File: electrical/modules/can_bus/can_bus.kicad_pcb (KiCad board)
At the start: 2 copper layers, 8 parts, among them U101 TCAN330DR

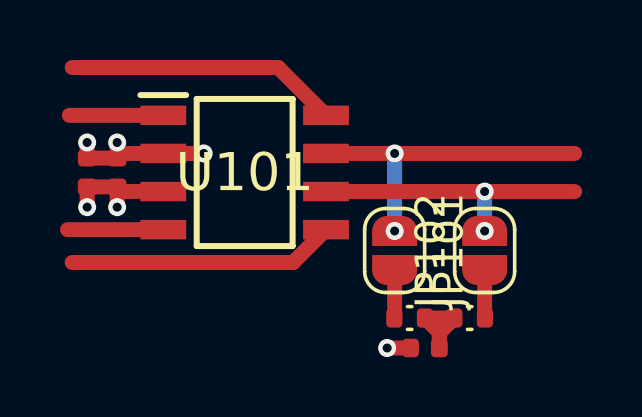
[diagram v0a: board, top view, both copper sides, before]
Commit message: Update CAN bus module and connect it.
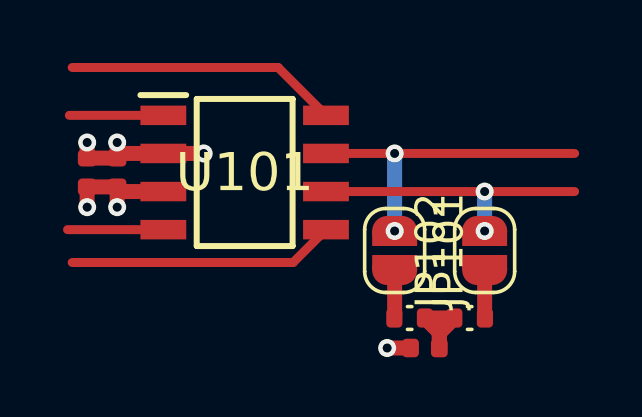
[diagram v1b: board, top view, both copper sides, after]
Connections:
- net +3V3 renamed /3V3
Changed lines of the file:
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@@
 	(net 0 "")
 	(net 1 "GND")
-	(net 2 "+3V3")
+	(net 2 "/3V3")
 	(net 3 "/CANH_TERMINATION")
 	(net 4 "/CANL_TERMINATION")
@@
 			(size 0.65 1.528)
 			(layers "F.Cu" "F.Mask" "F.Paste")
-			(net 2 "+3V3")
+			(net 2 "/3V3")
 			(pinfunction "VCC")
 			(pintype "passive")
@@
 			(layers "F.Cu" "F.Mask" "F.Paste")
 			(roundrect_rratio 0.25)
-			(net 2 "+3V3")
+			(net 2 "/3V3")
 			(pintype "passive")
 		)
@@
 			(layers "F.Cu" "F.Mask" "F.Paste")
 			(roundrect_rratio 0.25)
-			(net 2 "+3V3")
+			(net 2 "/3V3")
 			(pintype "passive")
 		)
@@
 		(start 144.339 98.58)
 		(end 141.145 98.58)
-		(width 0.5)
+		(width 0.3)
 		(layer "F.Cu")
 		(net 5)
@@
 		(start 148.166 93.175)
 		(end 141.3 93.175)
-		(width 0.5)
+		(width 0.3)
 		(layer "F.Cu")
 		(net 6)
@@
 		(start 149.761 94.77)
 		(end 148.166 93.175)
-		(width 0.5)
+		(width 0.3)
 		(layer "F.Cu")
 		(net 6)
@@
 		(start 149.761 98.58)
 		(end 148.666 99.675)
-		(width 0.5)
+		(width 0.3)
 		(layer "F.Cu")
 		(net 7)
@@
 		(start 148.666 99.675)
 		(end 141.3 99.675)
-		(width 0.5)
+		(width 0.3)
 		(layer "F.Cu")
 		(net 7)
@@
 		(start 144.339 94.77)
 		(end 141.205 94.77)
-		(width 0.5)
+		(width 0.3)
 		(layer "F.Cu")
 		(net 8)
@@
 		(start 152.05 96.04)
 		(end 158.05 96.04)
-		(width 0.5)
+		(width 0.3)
 		(layer "F.Cu")
 		(net 10)
@@
 		(start 149.761 96.04)
 		(end 152.05 96.04)
-		(width 0.5)
+		(width 0.3)
 		(layer "F.Cu")
 		(net 10)
@@
 		(start 155.05 97.31)
 		(end 158.05 97.31)
-		(width 0.5)
+		(width 0.3)
 		(layer "F.Cu")
 		(net 11)
@@
 		(start 149.761 97.31)
 		(end 155.05 97.31)
-		(width 0.5)
+		(width 0.3)
 		(layer "F.Cu")
 		(net 11)

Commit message: Complete fanout of CAN bus controller and related passive components.
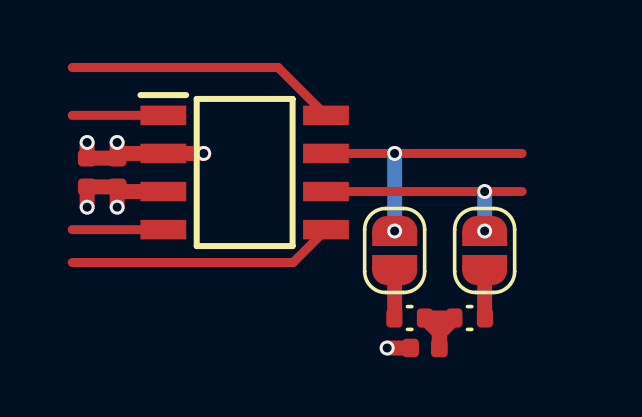
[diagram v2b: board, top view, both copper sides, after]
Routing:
- net /CANL: track 9.60 -> 7.85 mm
- net /CANH: track 10.9 -> 9.12 mm
- added copper zone on In2.Cu, net /3V3
- added copper zone on In1.Cu, net GND
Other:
- copper layers 2 -> 4

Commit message: Checkpoint work on building core board module.
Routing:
- net /CAN_SILENT: track 9.12 -> 6.66 mm
- net /CAN_SHUTDOWN: track 8.91 -> 6.66 mm
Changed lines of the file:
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@@
 	)
 	(segment
-		(start 148.166 93.175)
-		(end 141.3 93.175)
+		(start 149.761 94.77)
+		(end 148.666 93.675)
 		(width 0.3)
 		(layer "F.Cu")
@@
 	)
 	(segment
-		(start 149.761 94.77)
-		(end 148.166 93.175)
+		(start 148.666 93.675)
+		(end 143.55 93.675)
 		(width 0.3)
 		(layer "F.Cu")
@@
 	(segment
 		(start 148.666 99.675)
-		(end 141.3 99.675)
+		(end 143.55 99.675)
 		(width 0.3)
 		(layer "F.Cu")

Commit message: Restructure modules to get a reasonable core_board module.
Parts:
- C101, C102, C103, JP101, JP102, R101, R102, U101: moved to B.Cu
- moved C101 15.2 mm to (157.0, 96.7)
- moved C102 13.2 mm to (156.0, 96.7)
- moved JP102 11.3 mm to (143.8, 99.3)
- moved R102 10.3 mm to (144.3, 101.5), turned to 180 degrees
- moved C103 7.27 mm to (145.8, 102.5), turned to 180 degrees
- moved R101 6.25 mm to (146.3, 101.5), turned to 180 degrees
- moved JP101 5.25 mm to (146.8, 99.3)
- moved U101 4.75 mm to (151.8, 96.7), turned to 180 degrees

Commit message: Start sequence to synchronize UUIDs in modules so that ProjectInstances doesn't fail to import PCB layout.
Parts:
- renumbered C101 to C701, C102 to C702, C103 to C703, JP101 to JP701, JP102 to JP702, R101 to R701, R102 to R702, U101 to U701
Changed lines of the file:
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@@
 	(net 7 "/CAN_SHUTDOWN")
 	(net 8 "/CAN_TX")
-	(net 9 "Net-(C103-Pad2)")
+	(net 9 "Net-(C703-Pad2)")
 	(net 10 "/CANH")
 	(net 11 "/CANL")
@@
 		(descr "Capacitor SMD 0402 (1005 Metric), square (rectangular) end terminal, IPC_7351 nominal, (Body size source: IPC-SM-782 page 76, https://www.pcb-3d.com/wordpress/wp-content/uploads/ipc-sm-782a_amendment_1_and_2.pdf), generated with kicad-footprint-generator")
 		(tags "capacitor")
-		(property "Reference" "C103"
+		(property "Reference" "C703"
 			(at 0 1.16 0)
 			(layer "B.SilkS")
@@
 			(layers "B.Cu" "B.Mask" "B.Paste")
 			(roundrect_rratio 0.25)
-			(net 9 "Net-(C103-Pad2)")
+			(net 9 "Net-(C703-Pad2)")
 			(pintype "passive")
 		)
@@
 		(descr "SMD Solder Jumper, 1x1.5mm, rounded Pads, 0.3mm gap, open")
 		(tags "solder jumper open")
-		(property "Reference" "JP102"
+		(property "Reference" "JP702"
 			(at 0 0 0)
 			(layer "B.Fab")
@@
 		(descr "+soic d")
 		(tags "Integrated Circuit")
-		(property "Reference" "U101"
+		(property "Reference" "U701"
 			(at 0 0 0)
 			(layer "B.Fab")
@@
 		(descr "Capacitor SMD 0402 (1005 Metric), square (rectangular) end terminal, IPC_7351 nominal, (Body size source: IPC-SM-782 page 76, https://www.pcb-3d.com/wordpress/wp-content/uploads/ipc-sm-782a_amendment_1_and_2.pdf), generated with kicad-footprint-generator")
 		(tags "capacitor")
-		(property "Reference" "C102"
+		(property "Reference" "C702"
 			(at 0 1.16 90)
 			(layer "B.SilkS")
@@
 		(descr "Capacitor SMD 0402 (1005 Metric), square (rectangular) end terminal, IPC_7351 nominal, (Body size source: IPC-SM-782 page 76, https://www.pcb-3d.com/wordpress/wp-content/uploads/ipc-sm-782a_amendment_1_and_2.pdf), generated with kicad-footprint-generator")
 		(tags "capacitor")
-		(property "Reference" "C101"
+		(property "Reference" "C701"
 			(at 0 1.16 90)
 			(layer "B.SilkS")
@@
 		(descr "Resistor SMD 0402 (1005 Metric), square (rectangular) end terminal, IPC_7351 nominal, (Body size source: IPC-SM-782 page 72, https://www.pcb-3d.com/wordpress/wp-content/uploads/ipc-sm-782a_amendment_1_and_2.pdf), generated with kicad-footprint-generator")
 		(tags "resistor")
-		(property "Reference" "R101"
+		(property "Reference" "R701"
 			(at 0 1.17 0)
 			(layer "B.SilkS")
@@
 			(layers "B.Cu" "B.Mask" "B.Paste")
 			(roundrect_rratio 0.25)
-			(net 9 "Net-(C103-Pad2)")
+			(net 9 "Net-(C703-Pad2)")
 			(pintype "passive")
 		)
@@
 		(descr "SMD Solder Jumper, 1x1.5mm, rounded Pads, 0.3mm gap, open")
 		(tags "solder jumper open")
-		(property "Reference" "JP101"
+		(property "Reference" "JP701"
 			(at 0 0 0)
 			(layer "B.Fab")
@@
 		(descr "Resistor SMD 0402 (1005 Metric), square (rectangular) end terminal, IPC_7351 nominal, (Body size source: IPC-SM-782 page 72, https://www.pcb-3d.com/wordpress/wp-content/uploads/ipc-sm-782a_amendment_1_and_2.pdf), generated with kicad-footprint-generator")
 		(tags "resistor")
-		(property "Reference" "R102"
+		(property "Reference" "R702"
 			(at 0 1.17 0)
 			(layer "B.SilkS")
@@
 			(layers "B.Cu" "B.Mask" "B.Paste")
 			(roundrect_rratio 0.25)
-			(net 9 "Net-(C103-Pad2)")
+			(net 9 "Net-(C703-Pad2)")
 			(pintype "passive")
 		)
